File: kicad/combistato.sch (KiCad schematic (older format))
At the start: 5 parts

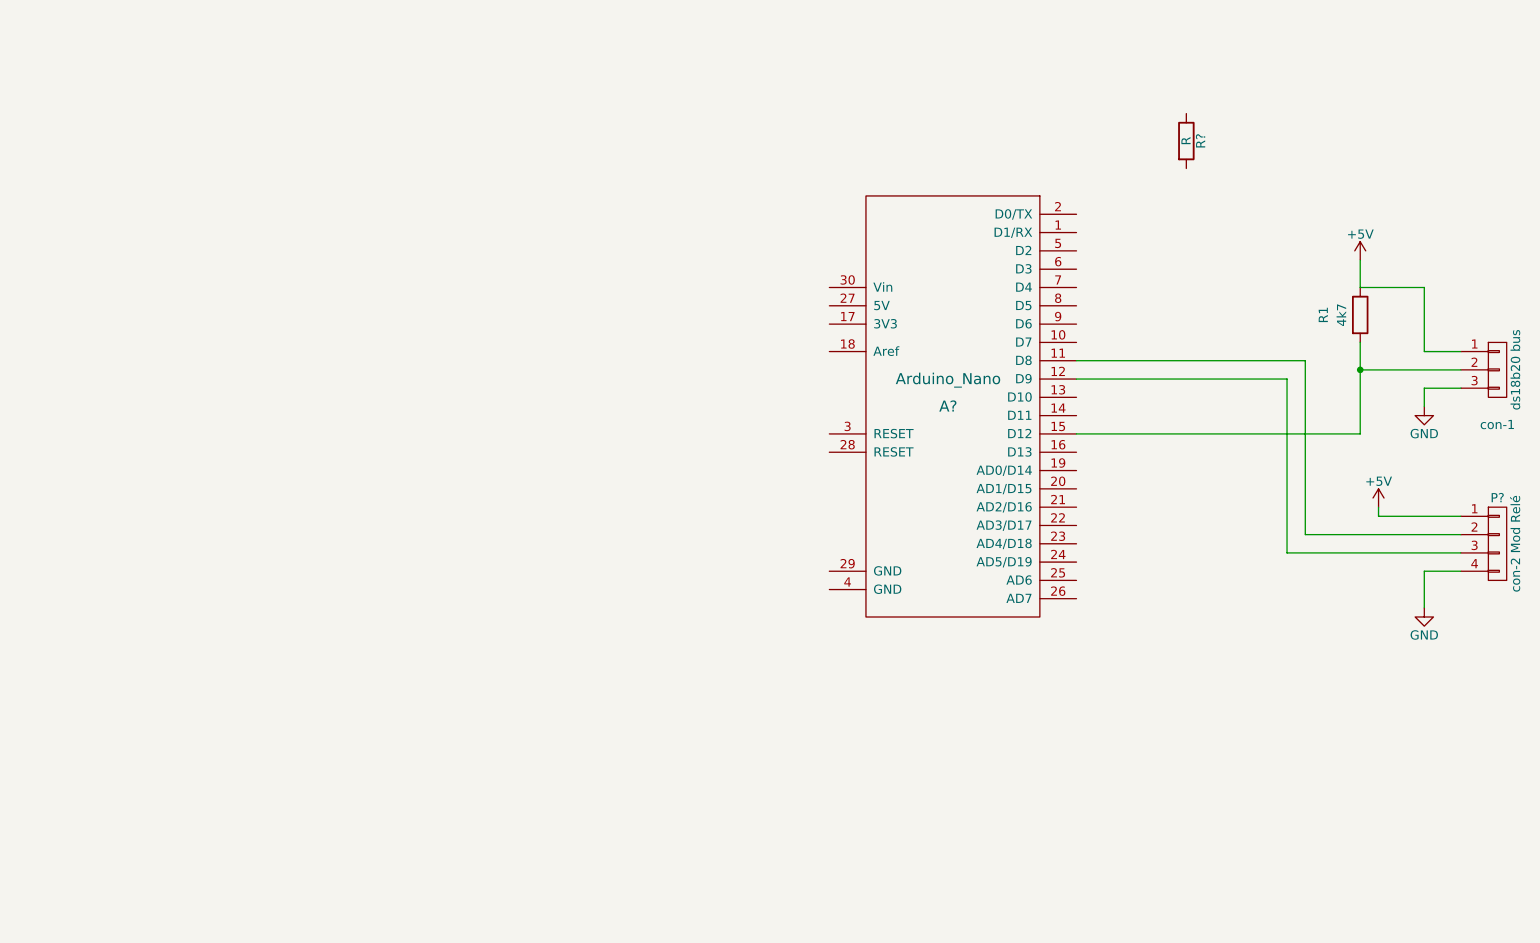
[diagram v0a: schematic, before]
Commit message: edicion de kicad para diagrama de circuito
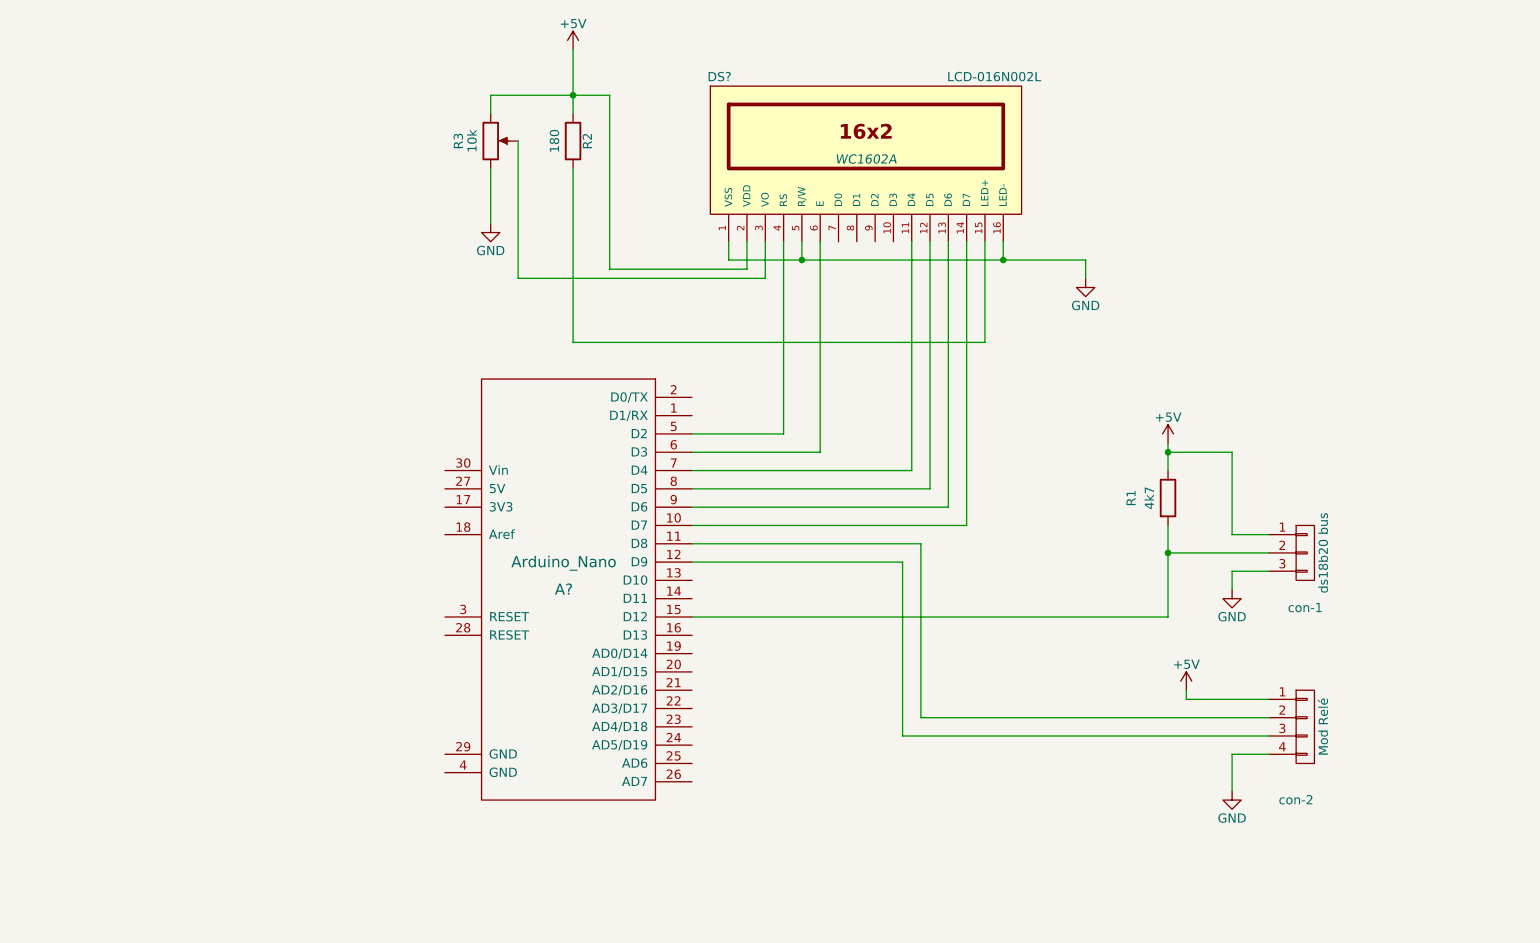
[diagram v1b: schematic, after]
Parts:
- added DS?: LCD-016N002L, WC1602A, symbol LCD-016N002L
- added R3: 10k, symbol POT
- R2: renamed from R?; value R -> 180
- con-2: renamed from P?; value con-2 Mod Relé -> Mod Relé
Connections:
- net +5V: now also R2.1, DS?.2 (VDD), R3.1
- net GND: now also DS?.1 (VSS), DS?.16 (LED-), DS?.5 (R/W), R3.3
- net at A?.10 (D7): now also DS?.14 (D7)
- net at A?.5 (D2): now also DS?.4 (RS)
- net at A?.6 (D3): now also DS?.6 (E)
- net at A?.7 (D4): now also DS?.11 (D4)
- net at A?.8 (D5): now also DS?.12 (D5)
- net at A?.9 (D6): now also DS?.13 (D6)
- net at R2.2: now also DS?.15 (LED+)
- new net: DS?.3 (VO), R3.2
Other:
- moved on the sheet: A?, R1, R2, con-1, con-2

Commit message: trabajo en pcb, circuitos, etc
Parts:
- removed A?: Arduino_Nano, symbol Arduino_Nano
- added A1: Arduino_Nano, Arduino Nano:arduino_nano, symbol Arduino_Nano
- added R10, R11, R9: 1k5, Resistores convencionales:R_Axial_DIN0411_L9.9mm_D3.6mm_P12.70mm_Horizontal, symbol R
- added R4, R5, R6, R8: 390, Resistores convencionales:R_Axial_DIN0411_L9.9mm_D3.6mm_P12.70mm_Horizontal, symbol R
- added R7: 4k7, Resistores convencionales:R_Axial_DIN0411_L9.9mm_D3.6mm_P12.70mm_Horizontal, symbol R
- added con3: 4x4keypad, Pin_Headers:Pin_Header_Angled_1x08, symbol CONN_01X08
- added con4: power, Pin_Headers:Pin_Header_Angled_1x03, symbol CONN_01X03
- DS1: renamed from DS?; footprint WC1602A -> LCD 1602:wc1602
- R1, R2: footprint (none) -> Resistores convencionales:R_Axial_DIN0411_L9.9mm_D3.6mm_P12.70mm_Horizontal
- R3: footprint (none) -> Potentiometers:Potentiometer_Bourns_3339H_Angular_ScrewUp
- con-1: footprint (none) -> Pin_Headers:Pin_Header_Angled_1x03
- con-2: footprint (none) -> Pin_Headers:Pin_Header_Angled_1x04
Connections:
- net +5V: now also con-1.3 (P3), con-2.4 (P4), R7.1, con4.3 (P3); no longer con-1.1 (P1), con-2.1 (P1)
- net GND: now also con-1.1 (P1), con-2.1 (P1), R9.1, con3.1 (P1), con4.1 (P1); no longer con-1.3 (P3), con-2.4 (P4)
- net at DS1.14 (D7): now also A1.10 (D7)
- net at con-2.2 (P2): now also A1.12 (D9)
- net at con-2.3 (P3): now also A1.11 (D8)
- net at R1.2, con-1.2 (P2): now also A1.15 (D12)
- net at DS1.4 (RS): now also A1.5 (D2)
- net at DS1.6 (E): now also A1.6 (D3)
- net at DS1.11 (D4): now also A1.7 (D4)
- net at DS1.12 (D5): now also A1.8 (D5)
- net at DS1.13 (D6): now also A1.9 (D6)
- new net: R10.1, R9.2, con3.2 (P2)
- new net: R10.2, R11.1, con3.3 (P3)
- new net: R11.2, con3.4 (P4)
- new net: R6.1, R7.2, R8.1, con3.5 (P5)
- new net: R5.1, R6.2, con3.6 (P6)
- new net: R4.1, R5.2, con3.7 (P7)
- new net: R4.2, con3.8 (P8)
- new net: A1.19 (AD0/D14), R8.2
- new net: A1.30 (Vin), con4.2 (P2)
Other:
- moved on the sheet: DS1, R1, R2, R3, con-1, con-2

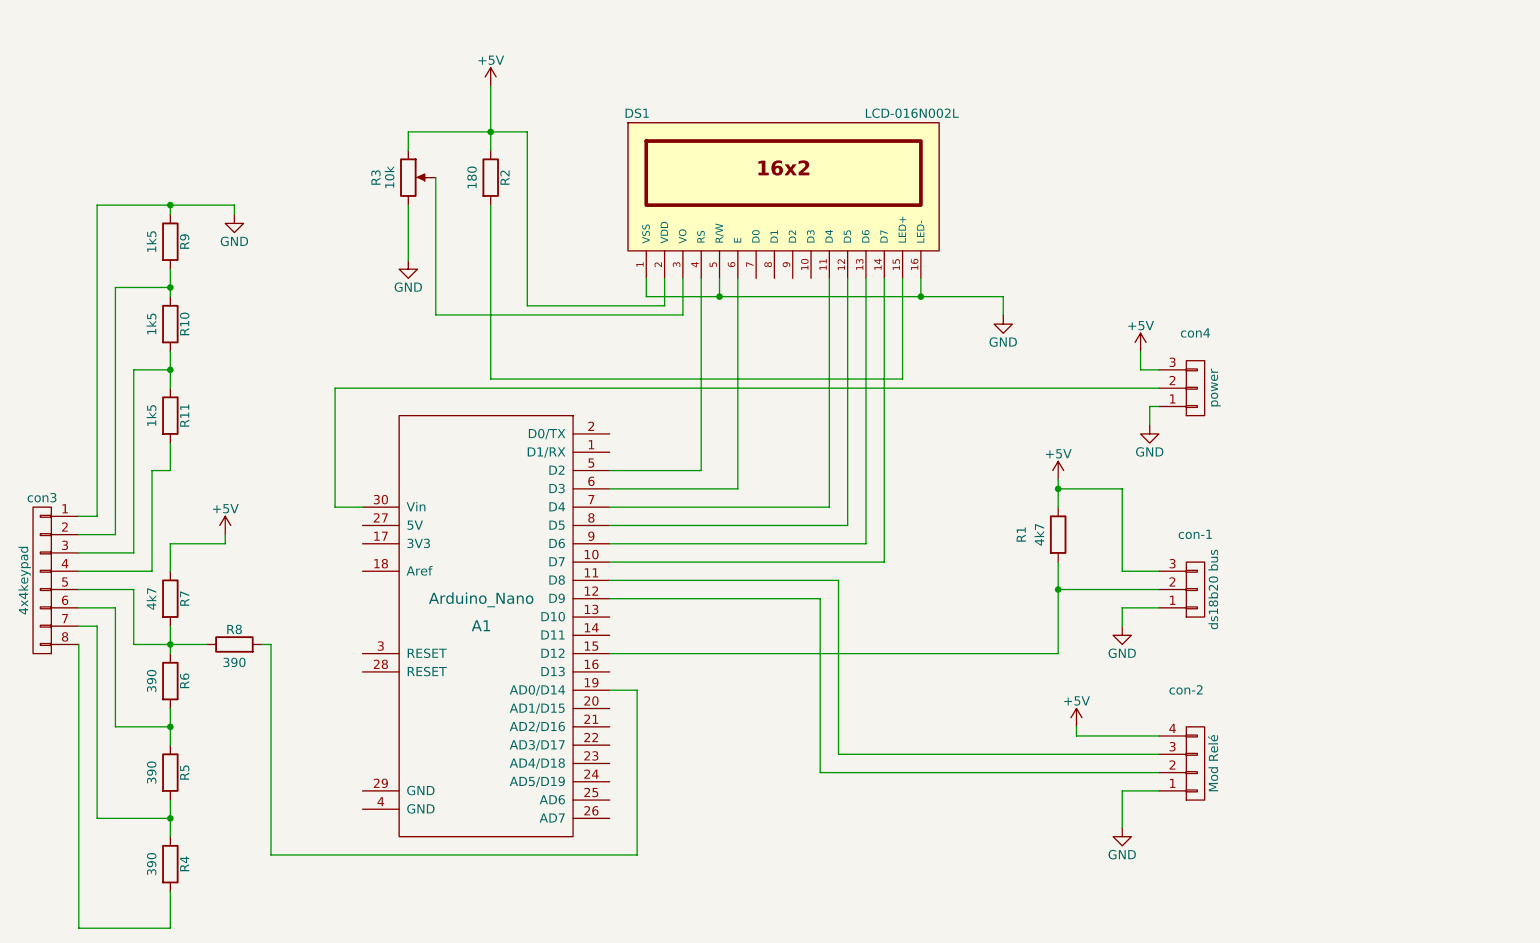
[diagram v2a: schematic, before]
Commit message: trabajando en pcb, esquema de circuito y otros
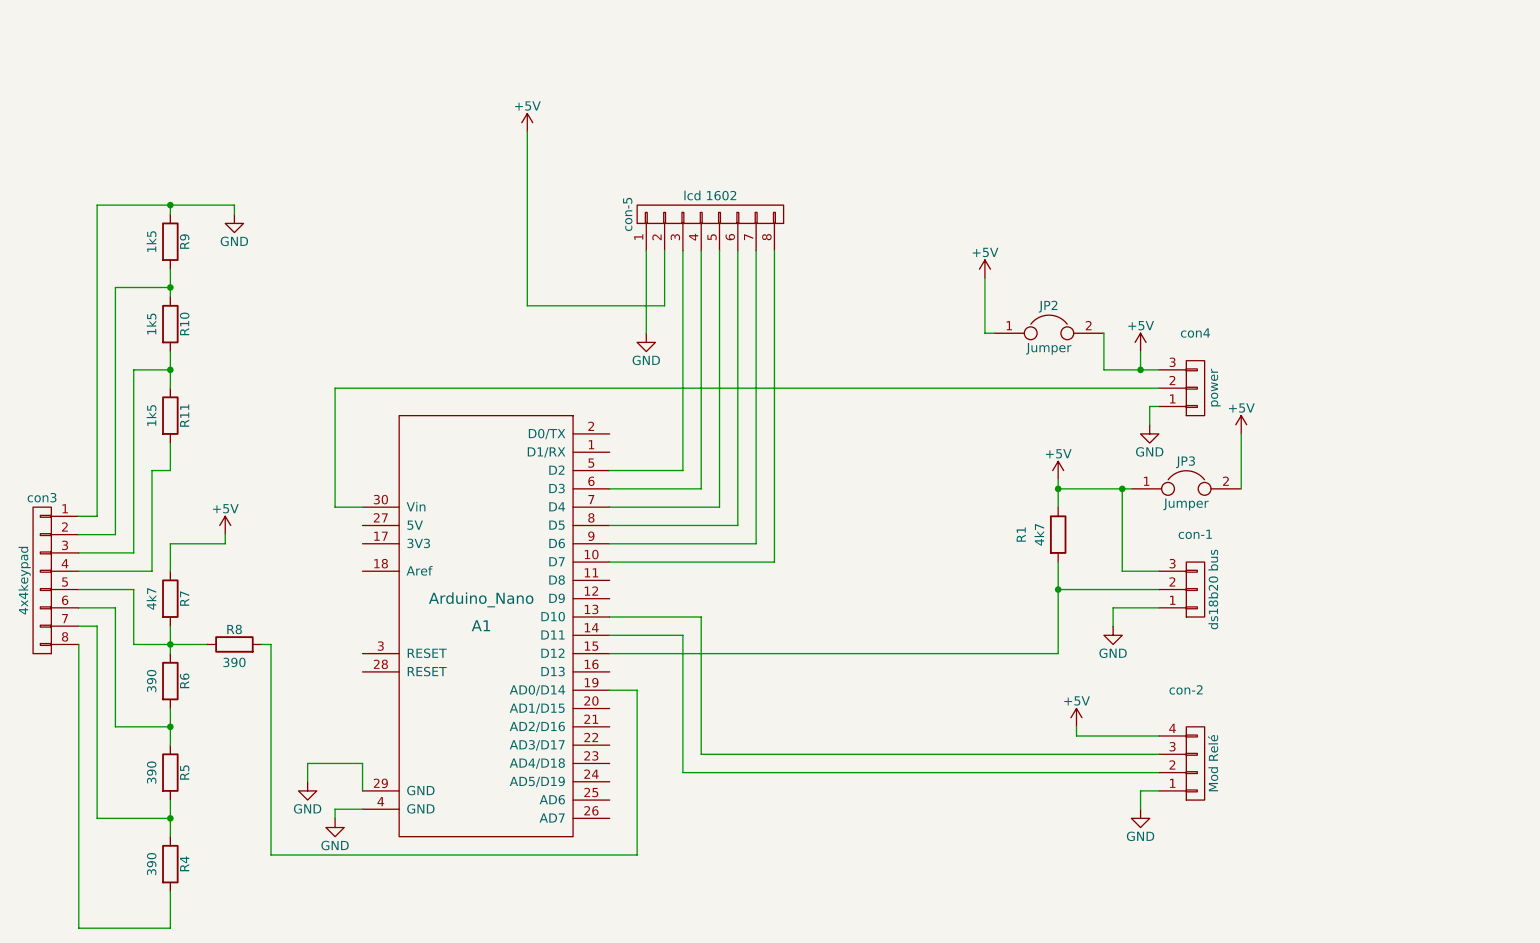
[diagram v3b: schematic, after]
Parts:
- removed DS1: LCD-016N002L, LCD 1602:wc1602, symbol LCD-016N002L
- removed R2: 180, Resistores convencionales:R_Axial_DIN0411_L9.9mm_D3.6mm_P12.70mm_Horizontal, symbol R
- removed R3: 10k, Potentiometers:Potentiometer_Bourns_3339H_Angular_ScrewUp, symbol POT
- added JP2, JP3: Jumper, Resistores convencionales:R_Axial_DIN0411_L9.9mm_D3.6mm_P12.70mm_Horizontal, symbol Jumper
- added con-5: lcd 1602, Pin_Headers:Pin_Header_Angled_1x08, symbol CONN_01X08
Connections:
- net +5V: now also JP2.1, JP2.2, JP3.1, JP3.2, con-5.2 (P2)
- net GND: now also A1.29 (GND), A1.4 (GND), con-5.1 (P1)
- net at con-2.2 (P2): now also A1.14 (D11); no longer A1.12 (D9)
- net at con-2.3 (P3): now also A1.13 (D10); no longer A1.11 (D8)
- net at A1.7 (D4): now also con-5.5 (P5)
- net at A1.8 (D5): now also con-5.6 (P6)
- net at A1.9 (D6): now also con-5.7 (P7)
- net at A1.10 (D7): now also con-5.8 (P8)
- net at A1.5 (D2): now also con-5.3 (P3)
- net at A1.6 (D3): now also con-5.4 (P4)
